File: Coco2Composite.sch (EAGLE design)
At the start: 21 parts, among them J1 TO_COCO2, J2 JACK_CONN1, J3 JACK_CONN2, J4 JACK_CONN3, J5 JACK_CONN4, J6 OUT_JACK, Q1 BC557, Q2 BC547, U1 MC1372

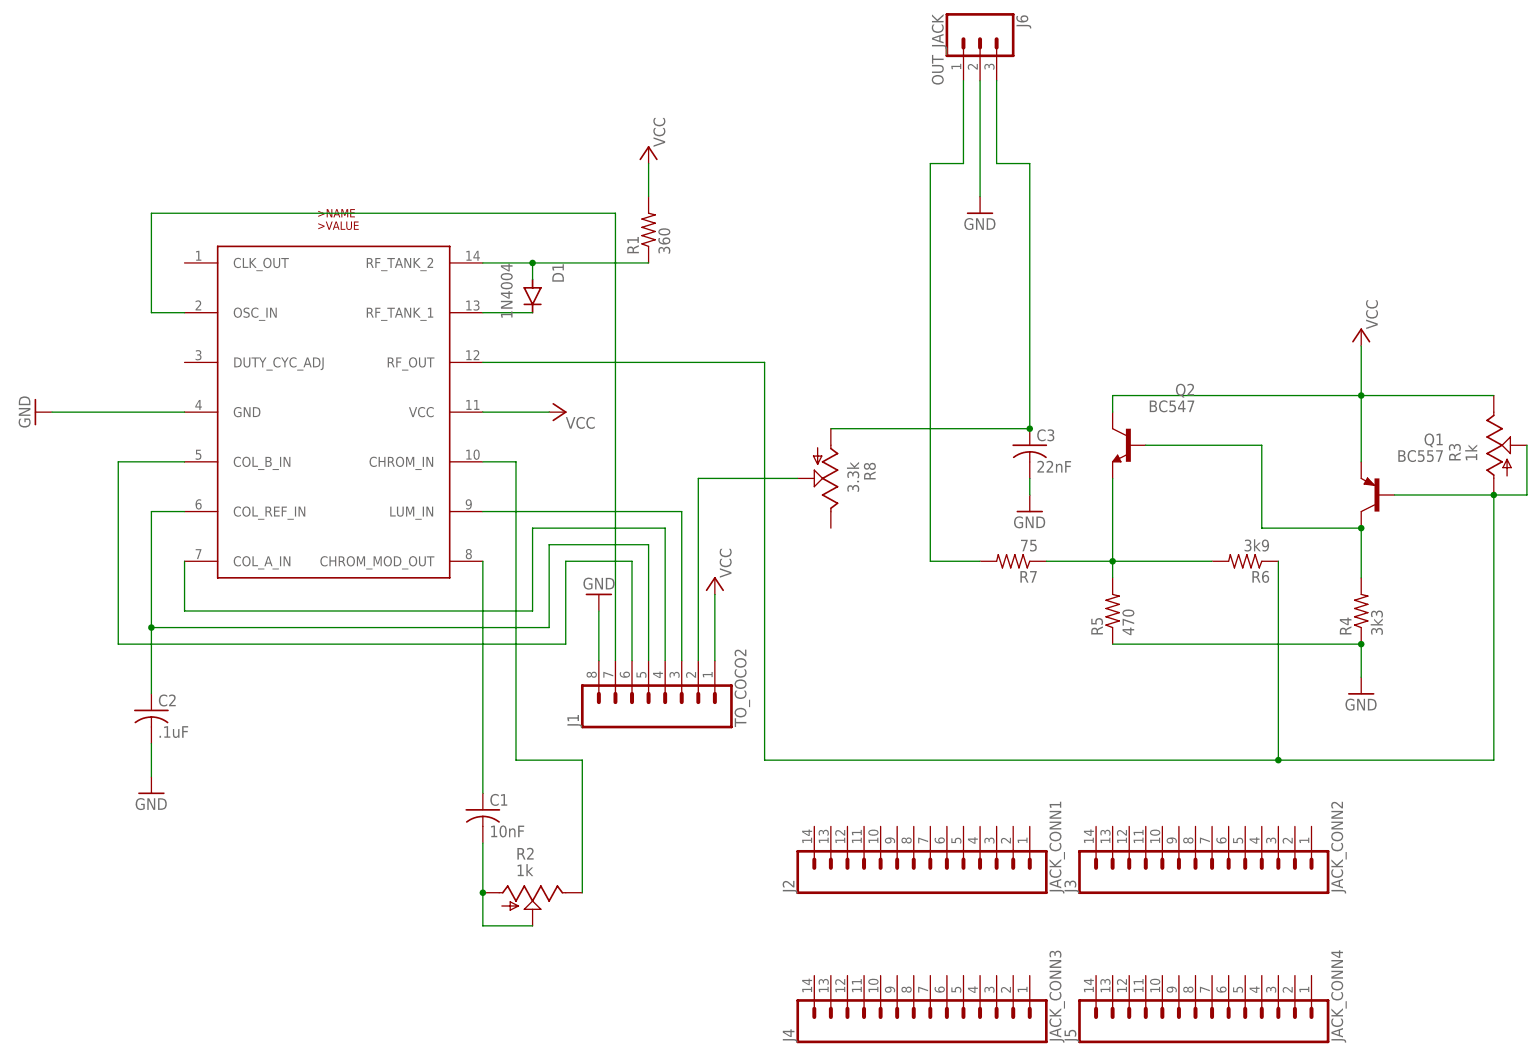
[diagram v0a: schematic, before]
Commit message: Tried making a version for the horizontal RF mod
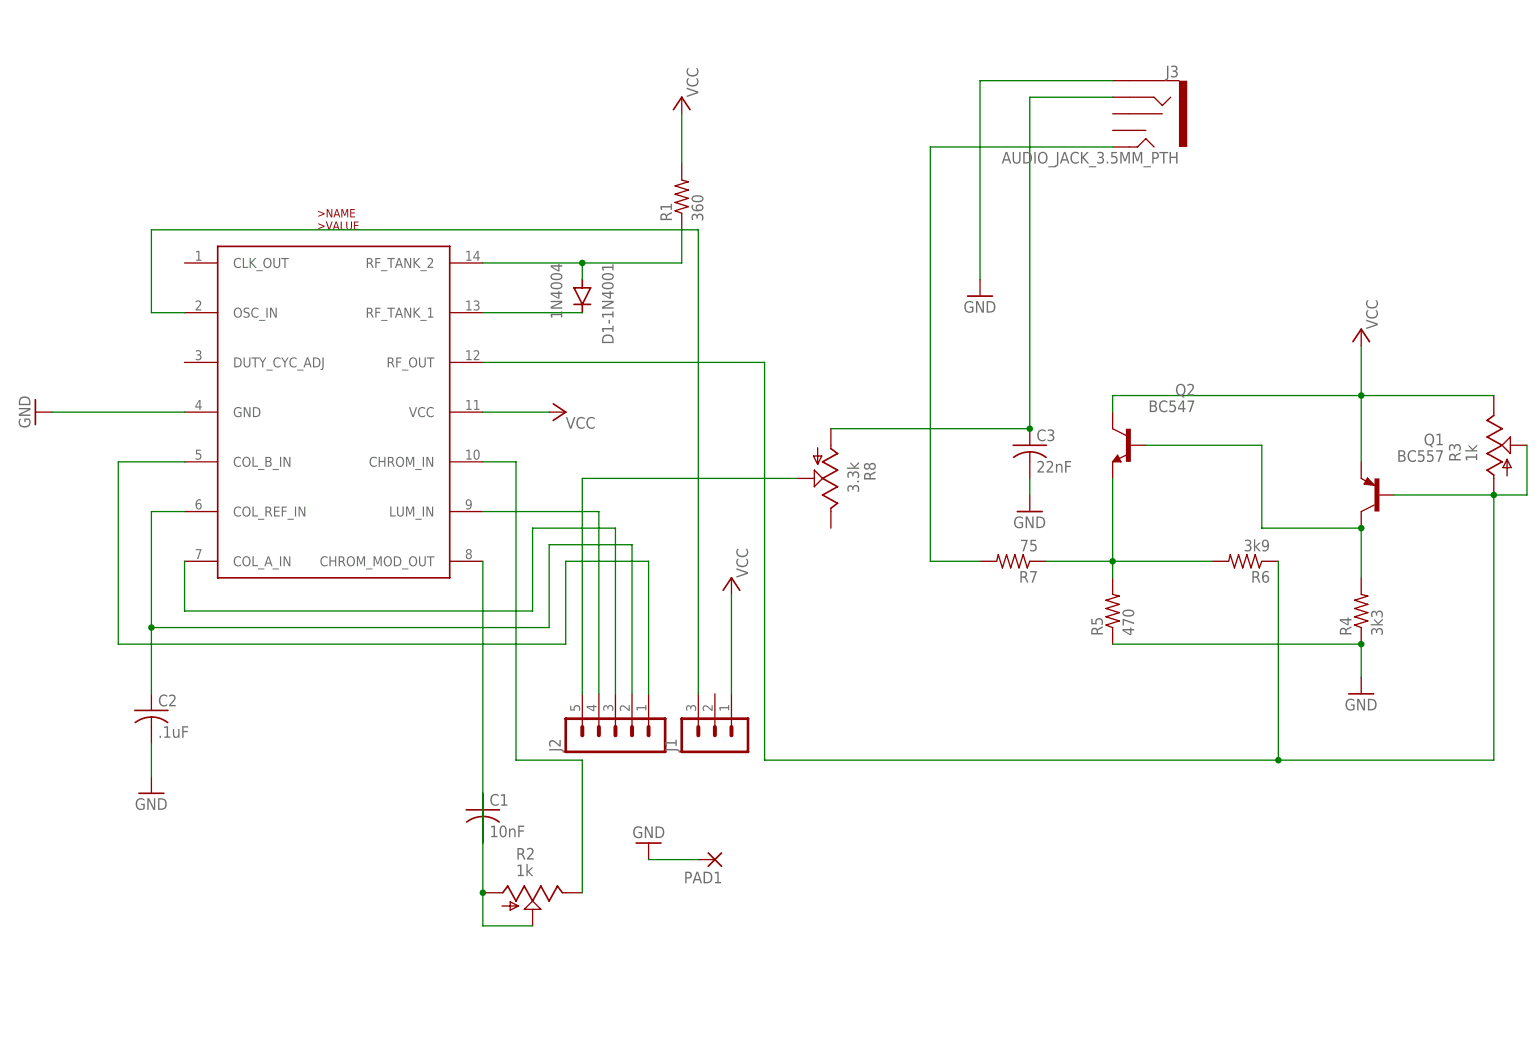
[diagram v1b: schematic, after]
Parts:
- removed D1: 1N4004, diode:1N4004
- removed J4: JACK_CONN3, SparkFun-Connectors:CONN_14
- removed J5: JACK_CONN4, SparkFun-Connectors:CONN_14
- removed J6: OUT_JACK, SparkFun-Connectors:CONN_03
- added D1-1N4001: 1N4004, diode:1N4004
- added PAD1: (no value), wirepad:2,54/0,8
- J1: value TO_COCO2 -> (none); device SparkFun-Connectors:CONN_08" -> con-lstb:MA03-1
- J2: value JACK_CONN1 -> (none); device SparkFun-Connectors:CONN_14 -> con-lstb:MA05-1
- J3: value JACK_CONN2 -> AUDIO_JACK_3.5MM_PTH; device SparkFun-Connectors:CONN_14 -> SparkFun-Connectors:AUDIO_JACK_3.5MM_PTH
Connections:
- net CHB: now also J2.2; no longer J1.5
- net CLK: now also J1.3; no longer J1.7
- net GND: now also J3.SLEEVE, PAD1.P; no longer J1.8, J6.2
- net N$1: now also D1-1N4001.C; no longer D1.C
- net N$10: now also J3.RING; no longer J6.3
- net N$2: now also D1-1N4001.A; no longer D1.A
- net N$3: now also C1.2; no longer C1.1
- net N$4: now also C1.1; no longer C1.2
- net N$9: now also J3.TIP; no longer J6.1
- net PHIB: now also J2.1; no longer J1.6
- net PHI_A: now also J2.3; no longer J1.4
- net SND: now also J2.5; no longer J1.2
- net Y: now also J2.4; no longer J1.3
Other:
- moved on the sheet: R1
